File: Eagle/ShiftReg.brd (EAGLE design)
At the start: 100 x 80 mm, 194 parts, among them Q100 310mA/60V/1.6Ω, Q101 310mA/60V/1.6Ω, Q102 310mA/60V/1.6Ω, Q103 310mA/60V/1.6Ω, Q104 310mA/60V/1.6Ω, Q105 310mA/60V/1.6Ω, Q106 310mA/60V/1.6Ω, Q107 310mA/60V/1.6Ω, Q108 310mA/60V/1.6Ω, Q109 310mA/60V/1.6Ω, Q110 310mA/60V/1.6Ω, Q111 310mA/60V/1.6Ω, Q112 310mA/60V/1.6Ω, Q113 310mA/60V/1.6Ω, Q114 310mA/60V/1.6Ω, Q115 310mA/60V/1.6Ω, Q116 310mA/60V/1.6Ω, Q117 310mA/60V/1.6Ω, Q118 310mA/60V/1.6Ω, Q119 310mA/60V/1.6Ω, Q120 310mA/60V/1.6Ω, Q121 310mA/60V/1.6Ω, Q122 310mA/60V/1.6Ω, Q123 310mA/60V/1.6Ω, Q124 310mA/60V/1.6Ω, Q125 310mA/60V/1.6Ω, Q126 310mA/60V/1.6Ω, Q127 310mA/60V/1.6Ω, Q128 310mA/60V/1.6Ω, Q129 310mA/60V/1.6Ω, Q130 310mA/60V/1.6Ω, Q131 310mA/60V/1.6Ω, Q132 310mA/60V/1.6Ω, Q166 310mA/60V/1.6Ω, Q167 310mA/60V/1.6Ω, Q168 310mA/60V/1.6Ω, Q169 310mA/60V/1.6Ω, Q170 310mA/60V/1.6Ω, Q171 310mA/60V/1.6Ω, Q172 310mA/60V/1.6Ω, Q173 310mA/60V/1.6Ω, Q174 310mA/60V/1.6Ω, Q175 310mA/60V/1.6Ω, Q176 310mA/60V/1.6Ω, Q177 310mA/60V/1.6Ω, Q178 310mA/60V/1.6Ω, Q179 310mA/60V/1.6Ω, Q180 310mA/60V/1.6Ω, Q181 310mA/60V/1.6Ω, Q182 310mA/60V/1.6Ω, Q183 310mA/60V/1.6Ω, Q184 310mA/60V/1.6Ω, Q185 310mA/60V/1.6Ω, Q186 310mA/60V/1.6Ω, Q187 310mA/60V/1.6Ω, Q188 310mA/60V/1.6Ω, Q189 310mA/60V/1.6Ω, Q190 310mA/60V/1.6Ω, Q191 310mA/60V/1.6Ω, Q192 310mA/60V/1.6Ω, Q193 310mA/60V/1.6Ω, Q194 310mA/60V/1.6Ω, Q195 310mA/60V/1.6Ω, Q196 310mA/60V/1.6Ω, Q197 310mA/60V/1.6Ω, Q198 310mA/60V/1.6Ω, Q232 310mA/60V/1.6Ω, Q233 310mA/60V/1.6Ω, Q234 310mA/60V/1.6Ω, Q235 310mA/60V/1.6Ω, Q236 310mA/60V/1.6Ω, Q237 310mA/60V/1.6Ω, Q238 310mA/60V/1.6Ω, Q239 310mA/60V/1.6Ω, Q240 310mA/60V/1.6Ω, Q241 310mA/60V/1.6Ω, Q242 310mA/60V/1.6Ω, Q243 310mA/60V/1.6Ω, Q244 310mA/60V/1.6Ω, Q245 310mA/60V/1.6Ω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

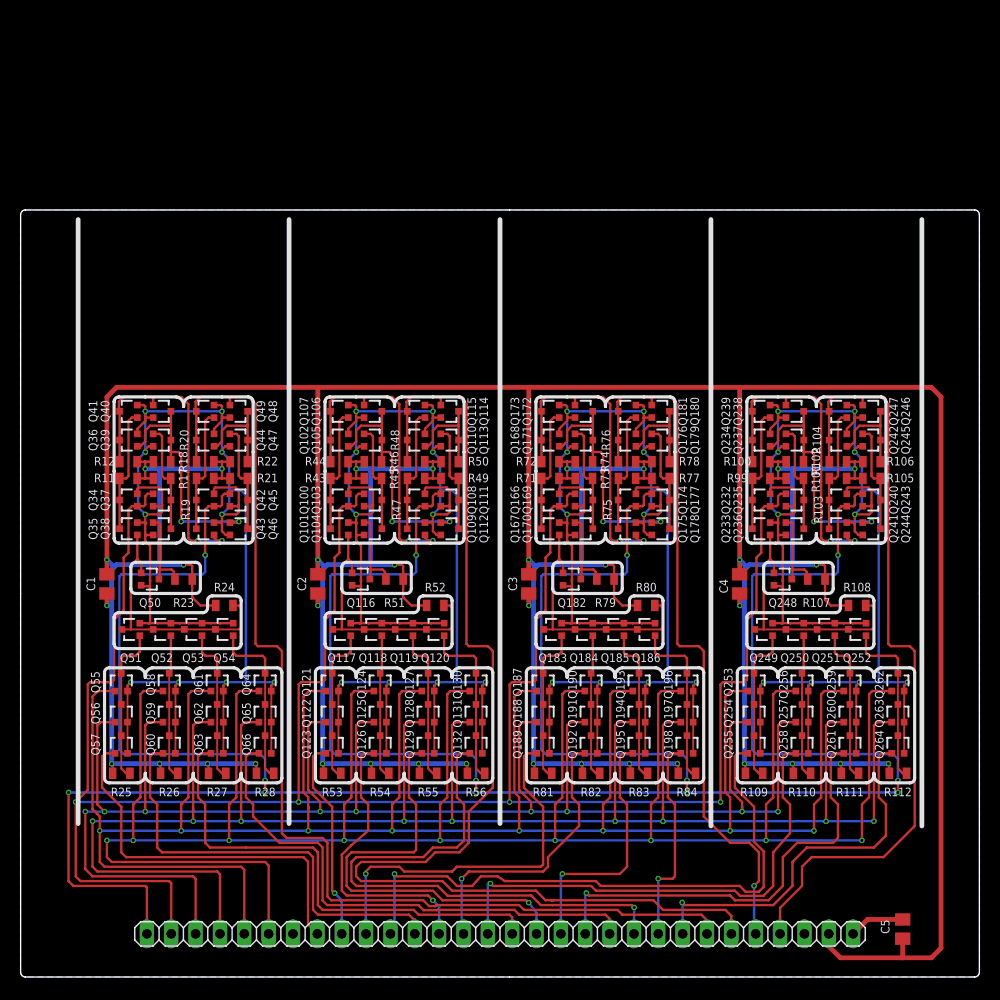
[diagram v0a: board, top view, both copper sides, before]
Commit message: Rerouted for SOT23
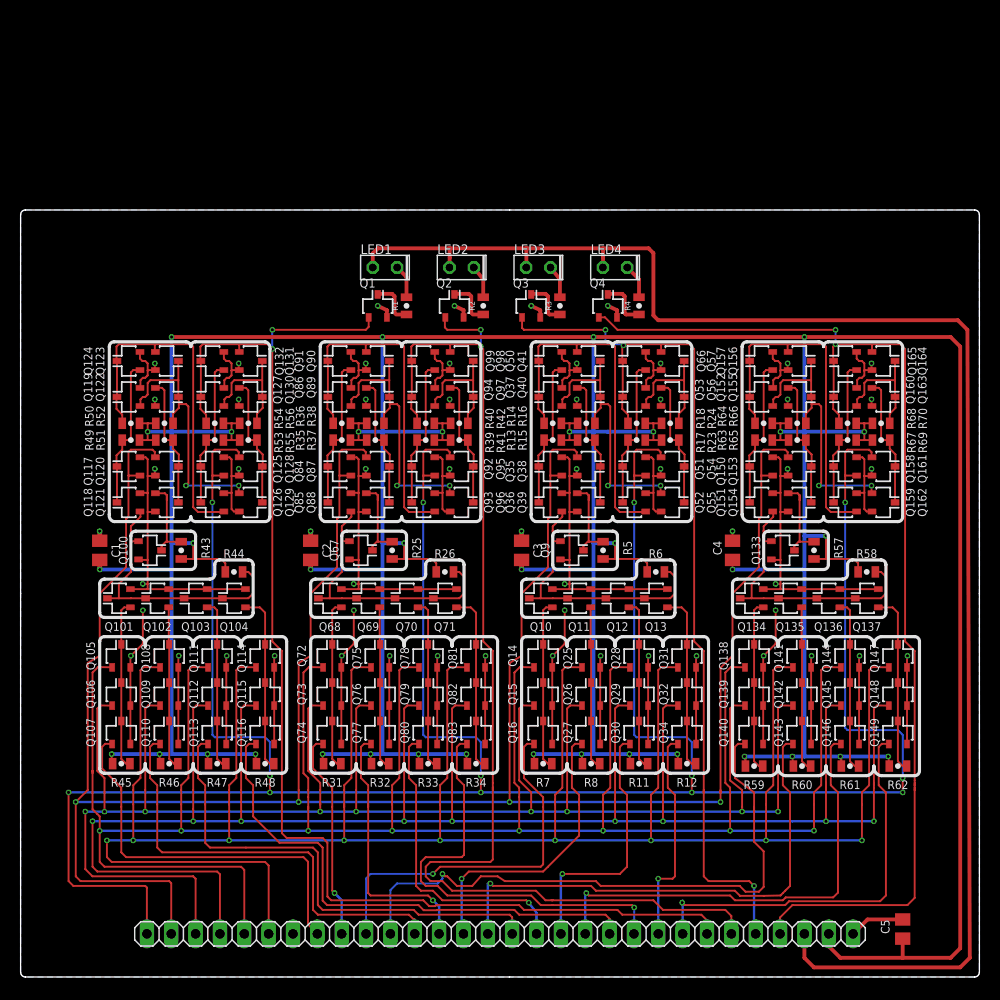
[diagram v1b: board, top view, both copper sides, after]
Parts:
- removed Q166, Q167, Q168, Q169, Q170, Q171, Q172, Q173, Q174, Q175, Q176, Q177, Q178, Q179, Q180, Q181, Q182, Q183, Q184, Q185, Q186, Q187, Q188, Q189, Q190, Q191, Q192, Q193, Q194, Q195, Q196, Q197, Q198, Q232, Q233, Q234, Q235, Q236, Q237, Q238, Q239, Q240, Q241, Q242, Q243, Q244, Q245, Q246, Q247, Q248, Q249, Q250, Q251, Q252, Q253, Q254, Q255, Q256, Q257, Q258, Q259, Q260, Q261, Q262, Q263, Q264, Q42, Q43, Q44, Q45, Q46, Q47, Q48, Q49, Q58, Q59, Q60, Q61, Q62, Q63, Q64, Q65: 310mA/60V/1.6Ω, SparkFun-DiscreteSemi:SOT323
- removed R100, R101, R102, R103, R104, R105, R106, R107, R108, R109, R110, R111, R112, R19, R20, R21, R22, R27, R28, R71, R72, R73, R74, R75, R76, R77, R78, R79, R80, R81, R82, R83, R84, R99: (no value), SparkFun-Resistors:0805
- added LED1, LED2, LED3, LED4: (no value), led:LED2X5
- added Q1, Q2, Q3, Q4: (no value), XSNOR:SOT23
- added Q10, Q11, Q12, Q13, Q133, Q134, Q135, Q136, Q137, Q138, Q139, Q14, Q140, Q141, Q142, Q143, Q144, Q145, Q146, Q147, Q148, Q149, Q15, Q150, Q151, Q152, Q153, Q154, Q155, Q156, Q157, Q158, Q159, Q16, Q160, Q161, Q162, Q163, Q164, Q165, Q25, Q26, Q27, Q28, Q29, Q30, Q31, Q32, Q67, Q68, Q69, Q70, Q71, Q72, Q73, Q74, Q75, Q76, Q77, Q78, Q79, Q80, Q81, Q82, Q83, Q84, Q85, Q86, Q87, Q88, Q89, Q9, Q90, Q91, Q92, Q93, Q94, Q95, Q96, Q97, Q98, Q99: 310mA/60V/1.6Ω, XSNOR:SOT23
- added R1, R13, R14, R15, R16, R2, R3, R31, R32, R33, R34, R35, R36, R37, R38, R39, R4, R40, R41, R42, R5, R57, R58, R59, R6, R60, R61, R62, R63, R64, R65, R66, R67, R68, R69, R7, R70, R8: (no value), XSNOR:0805
- Q100, Q101, Q102, Q103, Q104, Q105, Q106, Q107, Q108, Q109, Q110, Q111, Q112, Q113, Q114, Q115, Q116, Q117, Q118, Q119, Q120, Q121, Q122, Q123, Q124, Q125, Q126, Q127, Q128, Q129, Q130, Q131, Q132, Q34, Q35, Q36, Q37, Q38, Q39, Q40, Q41, Q50, Q51, Q52, Q53, Q54, Q55, Q56, Q57, Q66: device SparkFun-DiscreteSemi:SOT323 -> XSNOR:SOT23
- R11, R12, R17, R18, R23, R24, R25, R26, R43, R44, R45, R46, R47, R48, R49, R50, R51, R52, R53, R54, R55, R56: device SparkFun-Resistors:0805 -> XSNOR:0805
- moved Q57 70.0 mm to (68.0, 64.2), turned to 270 degrees
- moved Q56 66.3 mm to (68.0, 60.5), turned to 270 degrees
- moved R12 66.2 mm to (69.5, 22.2)
- moved Q34 63.1 mm to (69.5, 25.5), turned to 0 degrees
- moved R11 61.0 mm to (64.5, 22.2)
- moved Q55 60.5 mm to (68.0, 49.5), turned to 270 degrees
- moved Q66 55.5 mm to (64.0, 64.2), turned to 90 degrees
- moved Q51 55.2 mm to (64.0, 53.2)
- moved R23 52.8 mm to (67.8, 56.0)
- moved Q53 52.0 mm to (64.0, 60.5)
- moved Q52 51.0 mm to (64.0, 49.5)
- moved R24 50.2 mm to (67.8, 57.8), turned to 180 degrees
- moved Q54 49.7 mm to (68.0, 53.2), turned to 270 degrees
- moved R17 49.7 mm to (64.2, 56.0), turned to 0 degrees
- moved R18 49.7 mm to (64.2, 57.8), turned to 0 degrees
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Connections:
- removed net /Q0A1: Q36.1, Q39.3, Q40.3, Q46.1, R18.1
- removed net /Q0B: Q44.1, Q47.3, Q48.3, R22.1
- removed net /Q1A3: Q102.1, Q105.3, Q106.3, Q112.1, R46.1
- removed net /Q1B: Q110.1, Q113.3, Q114.3, R50.1
- removed net /Q2A5: Q168.1, Q171.3, Q172.3, Q178.1, R74.1
- removed net /Q2B: Q176.1, Q179.3, Q180.3, R78.1
- removed net /Q3A7: Q234.1, Q237.3, Q238.3, Q244.1, R102.1
- removed net /Q3B: Q242.1, Q245.3, Q246.3, R106.1
- removed net AUX1A': Q120.1, Q130.3, Q131.3, Q132.3, R56.2
- removed net LOAD1A': Q119.1, Q127.3, Q128.3, Q129.3, R55.2
- removed net N$116: Q243.3, Q244.3, Q245.1, R105.1
- removed net N$3: JP2.28
- removed net N$49: Q100.3, Q101.3, Q107.1, R43.1
- removed net N$50: Q103.3, Q104.3, Q105.1, R45.1
- removed net N$51: Q108.3, Q109.3, Q115.1, R47.1
- removed net N$52: Q111.3, Q112.3, Q113.1, R49.1
- removed net N$81: Q166.3, Q167.3, Q173.1, R71.1
- removed net N$82: Q169.3, Q170.3, Q171.1, R73.1
- removed net N$83: Q174.3, Q175.3, Q181.1, R75.1
- removed net N$84: Q177.3, Q178.3, Q179.1, R77.1
- removed net Q0A1: Q36.3, Q40.1, Q41.3, Q43.1, R12.1
- removed net Q1A3: Q102.3, Q106.1, Q107.3, Q109.1, R44.1
- removed net Q2A5: Q168.3, Q172.1, Q173.3, Q175.1, R72.1
- removed net Q3A7: Q234.3, Q238.1, Q239.3, Q241.1, R100.1
- removed net R0A: Q38.1, Q50.3, R23.2
- removed net S0A: Q35.1, Q50.1, Q51.3, Q52.3, Q53.3, Q54.3, R24.2
- new net AUX1A'-: Q71.1, Q81.3, Q82.3, Q83.3, R34.2
- new net LED+: JP2.28, LED1.A, LED2.A, LED3.A, LED4.A
- new net LOAD1A'-: Q70.1, Q78.3, Q79.3, Q80.3, R33.2
- new net N$10: Q92.3, Q93.3, Q99.1, R39.1
- new net N$100: Q119.3, Q123.1, Q124.3, Q126.1, R50.1
- new net N$101: Q119.1, Q122.3, Q123.3, Q129.1, R52.1
- new net N$102: Q127.1, Q130.3, Q131.3, R56.1
- new net N$103: Q86.1, Q89.3, Q90.3, Q96.1, R38.1
- new net N$104: Q86.3, Q90.1, Q91.3, Q93.1, R36.1
- new net N$105: Q94.1, Q97.3, Q98.3, R42.1
- new net N$11: Q95.3, Q96.3, Q97.1, R41.1
- new net N$110: Q53.1, Q56.3, Q57.3, R24.1
- new net N$111: Q37.1, Q40.3, Q41.3, Q55.1, R16.1
- new net N$112: Q37.3, Q41.1, Q50.3, Q52.1, R14.1
- new net N$12: Q150.3, Q151.3, Q157.1, R63.1
- new net N$13: Q153.3, Q154.3, Q155.1, R65.1
- new net N$14: Q158.3, Q159.3, Q165.1, R67.1
- new net N$15: Q161.3, Q162.3, Q163.1, R69.1
- new net N$16: Q117.3, Q118.3, Q124.1, R49.1
- new net N$17: Q120.3, Q121.3, Q122.1, R51.1
- new net N$18: Q125.3, Q126.3, Q132.1, R53.1
- new net N$19: Q128.3, Q129.3, Q130.1, R55.1
- new net N$2: Q38.3, Q39.3, Q40.1, R15.1
- new net N$20: Q3.3, R3.1
- new net N$21: Q4.3, R4.1
- new net N$22: LED4.K, R4.2
- new net N$23: LED3.K, R3.2
- new net N$24: LED2.K, R2.2
- new net N$25: LED1.K, R1.2
- new net N$7: Q54.3, Q55.3, Q56.1, R23.1
- new net N$8: Q84.3, Q85.3, Q91.1, R35.1
- new net N$9: Q87.3, Q88.3, Q89.1, R37.1
- new net R0A-: Q100.3, Q121.1, R43.2
- new net S0A-: Q100.1, Q101.3, Q102.3, Q103.3, Q104.3, Q118.1, R44.2
- net /CLK: now also Q117.1, Q120.1, Q150.1, Q153.1, Q35.1, Q38.1, Q84.1, Q87.1; no longer Q100.1, Q103.1, Q166.1, Q169.1, Q232.1, Q235.1, Q34.1, Q37.1
- net /OP1: now also Q112.1, Q115.1, Q145.1, Q148.1, Q29.1, Q32.1, Q79.1, Q82.1; no longer Q128.1, Q131.1, Q194.1, Q197.1, Q260.1, Q263.1, Q62.1, Q65.1
- net /OP2: now also Q108.1, Q114.1, Q141.1, Q147.1, Q25.1, Q31.1, Q75.1, Q81.1; no longer Q124.1, Q130.1, Q190.1, Q196.1, Q256.1, Q262.1, Q58.1, Q64.1
- net AUX0: now also Q116.1; no longer Q66.1
- net AUX0A': now also Q104.1, Q114.3, Q115.3, Q116.3, R48.2; no longer Q54.1, Q64.3, Q65.3, Q66.3, R28.2
- net AUX1: now also Q83.1; no longer Q132.1
- net AUX2: now also Q34.1; no longer Q198.1
- net AUX2A': now also Q13.1, Q31.3, Q32.3, Q34.3, R12.2; no longer Q186.1, Q196.3, Q197.3, Q198.3, R84.2
- net AUX3: now also Q149.1; no longer Q264.1
- net AUX3A': now also Q137.1, Q147.3, Q148.3, Q149.3, R62.2; no longer Q252.1, Q262.3, Q263.3, Q264.3, R112.2
- net CLK: now also Q125.1, Q128.1, Q158.1, Q161.1, Q51.1, Q54.1, Q92.1, Q95.1; no longer Q108.1, Q111.1, Q174.1, Q177.1, Q240.1, Q243.1, Q42.1, Q45.1
- net GND: now also Q1.2, Q10.2, Q11.2, Q12.2, Q13.2, Q133.2, Q134.2, Q135.2, Q136.2, Q137.2, Q138.2, Q139.2, Q14.2, Q140.2, Q141.2, Q142.2, Q143.2, Q144.2, Q145.2, Q146.2, Q147.2, Q148.2, Q149.2, Q15.2, Q150.2, Q151.2, Q152.2, Q153.2, Q154.2, Q155.2, Q156.2, Q157.2, Q158.2, Q159.2, Q16.2, Q160.2, Q161.2, Q162.2, Q163.2, Q164.2, Q165.2, Q2.2, Q25.2, Q26.2, Q27.2, Q28.2, Q29.2, Q3.2, Q30.2, Q31.2, Q32.2, Q4.2, Q67.2, Q68.2, Q69.2, Q70.2, Q71.2, Q72.2, Q73.2, Q74.2, Q75.2, Q76.2, Q77.2, Q78.2, Q79.2, Q80.2, Q81.2, Q82.2, Q83.2, Q84.2, Q85.2, Q86.2, Q87.2, Q88.2, Q89.2, Q9.2, Q90.2, Q91.2, Q92.2, Q93.2, Q94.2, Q95.2, Q96.2, Q97.2, Q98.2, Q99.2; no longer Q166.2, Q167.2, Q168.2, Q169.2, Q170.2, Q171.2, Q172.2, Q173.2, Q174.2, Q175.2, Q176.2, Q177.2, Q178.2, Q179.2, Q180.2, Q181.2, Q182.2, Q183.2, Q184.2, Q185.2, Q186.2, Q187.2, Q188.2, Q189.2, Q190.2, Q191.2, Q192.2, Q193.2, Q194.2, Q195.2, Q196.2, Q197.2, Q198.2, Q232.2, Q233.2, Q234.2, Q235.2, Q236.2, Q237.2, Q238.2, Q239.2, Q240.2, Q241.2, Q242.2, Q243.2, Q244.2, Q245.2, Q246.2, Q247.2, Q248.2, Q249.2, Q250.2, Q251.2, Q252.2, Q253.2, Q254.2, Q255.2, Q256.2, Q257.2, Q258.2, Q259.2, Q260.2, Q261.2, Q262.2, Q263.2, Q264.2, Q42.2, Q43.2, Q44.2, Q45.2, Q46.2, Q47.2, Q48.2, Q49.2, Q58.2, Q59.2, Q60.2, Q61.2, Q62.2, Q63.2, Q64.2, Q65.2
- net LOAD0: now also Q113.1; no longer Q63.1
- net LOAD0A': now also Q103.1, Q111.3, Q112.3, Q113.3, R47.2; no longer Q53.1, Q61.3, Q62.3, Q63.3, R27.2
- net LOAD1: now also Q80.1; no longer Q129.1
- net LOAD2: now also Q30.1; no longer Q195.1
- net LOAD2A': now also Q12.1, Q28.3, Q29.3, Q30.3, R11.2; no longer Q185.1, Q193.3, Q194.3, Q195.3, R83.2
- net LOAD3: now also Q146.1; no longer Q261.1
- net LOAD3A': now also Q136.1, Q144.3, Q145.3, Q146.3, R61.2; no longer Q251.1, Q259.3, Q260.3, Q261.3, R111.2
- net N$1: now also Q36.3, Q50.1, R13.1; no longer Q34.3, Q41.1, R11.1
- net N$113: now also Q160.1, Q163.3, Q164.3, R70.1; no longer Q232.3, Q233.3, Q239.1, R99.1
- net N$114: now also Q152.1, Q155.3, Q156.3, Q162.1, R66.1; no longer Q235.3, Q236.3, Q237.1, R101.1
- net N$115: now also Q152.3, Q156.1, Q157.3, Q159.1, R64.1; no longer Q240.3, Q241.3, Q247.1, R103.1
- net N$4: now also Q51.3, Q52.3, Q66.1; no longer Q37.3, Q38.3, Q39.1
- net N$5: now also Q1.3, R1.1; no longer Q42.3, Q43.3, Q49.1, R19.1
- net N$6: now also Q2.3, R2.1; no longer Q45.3, Q46.3, Q47.1, R21.1
- net NEXT0: now also Q110.1; no longer Q60.1
- net NEXT0A': now also Q102.1, Q108.3, Q109.3, Q110.3, R46.2; no longer Q52.1, Q58.3, Q59.3, Q60.3, R26.2
- net NEXT1: now also Q77.1; no longer Q126.1
- net NEXT1A': now also Q69.1, Q75.3, Q76.3, Q77.3, R32.2; no longer Q118.1, Q124.3, Q125.3, Q126.3, R54.2
- net NEXT2: now also Q27.1; no longer Q192.1
- net NEXT2A': now also Q11.1, Q25.3, Q26.3, Q27.3, R8.2; no longer Q184.1, Q190.3, Q191.3, Q192.3, R82.2
- net NEXT3: now also Q143.1; no longer Q258.1
- net NEXT3A': now also Q135.1, Q141.3, Q142.3, Q143.3, R60.2; no longer Q250.1, Q256.3, Q257.3, Q258.3, R110.2
- net OP1: now also Q106.1, Q109.1, Q139.1, Q142.1, Q15.1, Q26.1, Q73.1, Q76.1; no longer Q122.1, Q125.1, Q188.1, Q191.1, Q254.1, Q257.1, Q56.1, Q59.1
- net OP2: now also Q105.1, Q111.1, Q138.1, Q14.1, Q144.1, Q28.1, Q72.1, Q78.1; no longer Q121.1, Q127.1, Q187.1, Q193.1, Q253.1, Q259.1, Q55.1, Q61.1
- net OUT0: now also Q1.1, Q127.3, Q131.1, Q132.3, R54.1; no longer Q44.3, Q48.1, Q49.3, R20.1
- net OUT1: now also Q2.1, Q94.3, Q98.1, Q99.3, R40.1; no longer Q110.3, Q114.1, Q115.3, R48.1
- net OUT2: now also Q3.1, Q53.3, Q57.1, Q66.3, R18.1; no longer Q176.3, Q180.1, Q181.3, R76.1
- net OUT3: now also Q160.3, Q164.1, Q165.3, Q4.1, R68.1; no longer Q242.3, Q246.1, Q247.3, R104.1
- net PREV0: now also Q107.1; no longer Q57.1
- net PREV0A': now also Q101.1, Q105.3, Q106.3, Q107.3, R45.2; no longer Q51.1, Q55.3, Q56.3, Q57.3, R25.2
- net PREV1: now also Q74.1; no longer Q123.1
- net PREV1A': now also Q68.1, Q72.3, Q73.3, Q74.3, R31.2; no longer Q117.1, Q121.3, Q122.3, Q123.3, R53.2
- net PREV2: now also Q16.1; no longer Q189.1
- net PREV2A': now also Q10.1, Q14.3, Q15.3, Q16.3, R7.2; no longer Q183.1, Q187.3, Q188.3, Q189.3, R81.2
- net PREV3: now also Q140.1; no longer Q255.1
- net PREV3A': now also Q134.1, Q138.3, Q139.3, Q140.3, R59.2; no longer Q249.1, Q253.3, Q254.3, Q255.3, R109.2
- net R1A: now also Q67.3, Q88.1, R25.2; no longer Q104.1, Q116.3, R51.2
- net R2A: now also Q39.1, Q9.3, R5.2; no longer Q170.1, Q182.3, R79.2
- net R3A: now also Q133.3, Q154.1, R57.2; no longer Q236.1, Q248.3, R107.2
- net S1A: now also Q67.1, Q68.3, Q69.3, Q70.3, Q71.3, Q85.1, R26.2; no longer Q101.1, Q116.1, Q117.3, Q118.3, Q119.3, Q120.3, R52.2
- net S2A: now also Q10.3, Q11.3, Q12.3, Q13.3, Q36.1, Q9.1, R6.2; no longer Q167.1, Q182.1, Q183.3, Q184.3, Q185.3, Q186.3, R80.2
- net S3A: now also Q133.1, Q134.3, Q135.3, Q136.3, Q137.3, Q151.1, R58.2; no longer Q233.1, Q248.1, Q249.3, Q250.3, Q251.3, Q252.3, R108.2
- net VCC: now also R11.1, R12.1, R13.2, R14.2, R15.2, R16.2, R23.2, R24.2, R31.1, R32.1, R33.1, R34.1, R35.2, R36.2, R37.2, R38.2, R39.2, R40.2, R41.2, R42.2, R43.1, R44.1, R45.1, R46.1, R47.1, R48.1, R5.1, R51.2, R52.2, R53.2, R54.2, R55.2, R56.2, R57.1, R58.1, R59.1, R6.1, R60.1, R61.1, R62.1, R63.2, R64.2, R65.2, R66.2, R67.2, R68.2, R69.2, R7.1, R70.2, R8.1; no longer R100.2, R101.2, R102.2, R103.2, R104.2, R105.2, R106.2, R107.1, R108.1, R109.1, R11.2, R110.1, R111.1, R112.1, R12.2, R19.2, R20.2, R21.2, R22.2, R23.1, R24.1, R27.1, R28.1, R43.2, R44.2, R45.2, R46.2, R47.2, R48.2, R51.1, R52.1, R53.1, R54.1, R55.1, R56.1, R71.2, R72.2, R73.2, R74.2, R75.2, R76.2, R77.2, R78.2, R79.1, R80.1, R81.1, R82.1, R83.1, R84.1, R99.2
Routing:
- net GND: track 630.5 -> 403.3 mm, vias 44 -> 56
- net LED+: track 0.00 -> 163.1 mm
- net VCC: track 616.4 -> 564.1 mm, vias 32 -> 36
- net CLK: track 335.5 -> 292.7 mm
- net N$112: track 0.00 -> 37.6 mm
- net N$104: track 0.00 -> 37.6 mm
- net N$100: track 0.00 -> 37.6 mm
- net OUT3: track 82.0 -> 118.4 mm, vias 0 -> 2
- net Q2A5: track 34.1 -> 0.00 mm, vias 2 -> 0
- net Q1A3: track 34.1 -> 0.00 mm, vias 2 -> 0
- net Q0A1: track 34.1 -> 0.00 mm, vias 2 -> 0
- net Q3A7: track 34.1 -> 0.00 mm, vias 2 -> 0
- net S0A-: track 0.00 -> 29.4 mm
- net N$101: track 0.00 -> 28.8 mm, vias 0 -> 2
- net N$111: track 0.00 -> 28.8 mm, vias 0 -> 2
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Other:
- board text added: "Universal Shiftregister rev 1"

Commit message: Cleanups of PCBs
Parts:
- JP2: device pinhead:1X30 -> XSNOR:1X30
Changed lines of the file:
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@@
 </autorouter>
 <elements>
-<element name="JP2" library="pinhead" library_urn="urn:adsk.eagle:library:325" package="1X30" package3d_urn="urn:adsk.eagle:package:22460/2" value="" x="50" y="4.5" smashed="yes">
+<element name="JP2" library="XSNOR" library_urn="urn:adsk.eagle:library:1320997" package="1X30" package3d_urn="urn:adsk.eagle:package:1346145/1" value="" x="50" y="4.5" smashed="yes">
 <attribute name="VALUE" x="11.9" y="1.325" size="1.27" layer="27"/>
 </element>

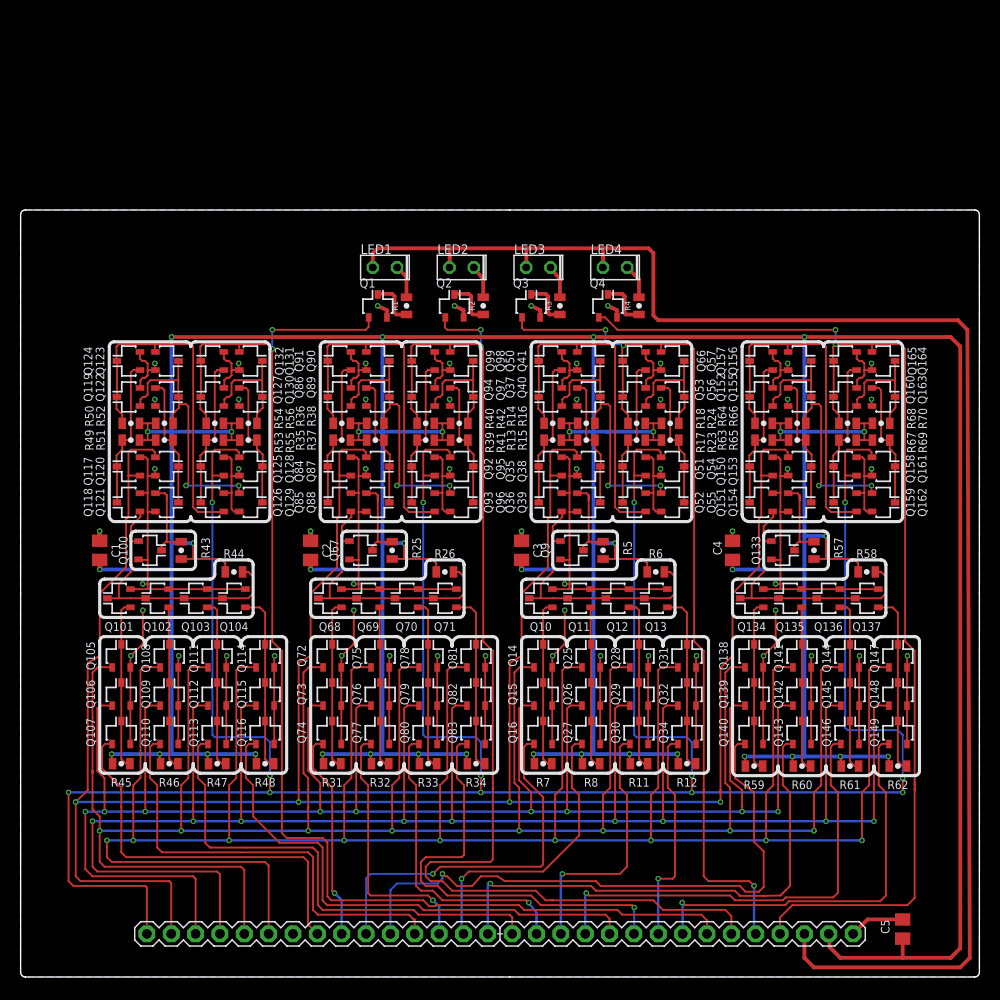
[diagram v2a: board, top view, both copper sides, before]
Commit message: Silk cleanup. Routing of GND instead of floodfill
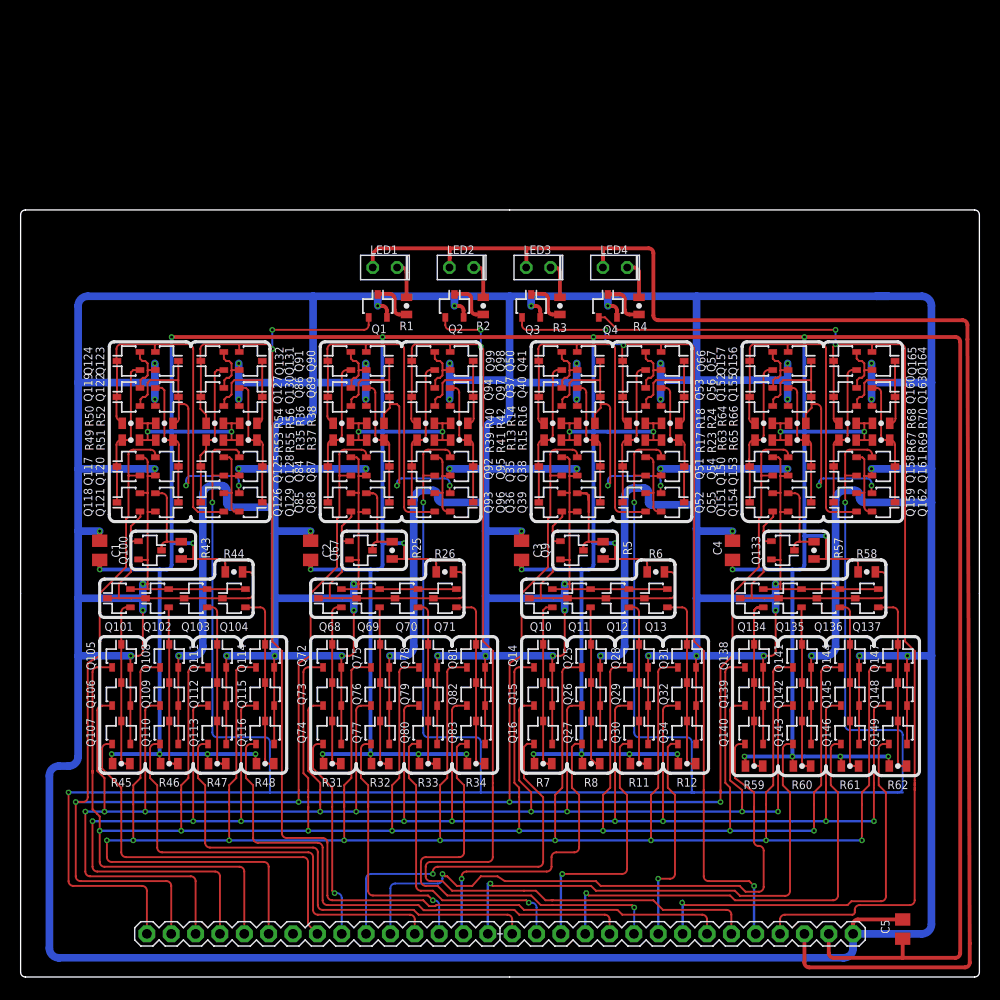
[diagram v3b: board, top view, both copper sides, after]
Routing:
- net GND: track 403.3 -> 1200.5 mm
- net PREV3A': track 17.9 -> 22.6 mm
- net R2A: track 9.32 -> 12.1 mm
- net CLK: track 292.7 -> 295.2 mm, vias 13 -> 5
- net NEXT2: track 30.7 -> 32.2 mm
- net N$101: track 28.8 -> 30.1 mm
- net N$111: track 28.8 -> 30.0 mm
- net /OP1: track 214.5 -> 213.3 mm
- net AUX0: track 55.2 -> 56.3 mm
- net OP1: track 197.8 -> 196.8 mm
- net N$103: track 28.8 -> 29.7 mm
- net LED+: track 163.1 -> 164.0 mm
- net /OP2: track 267.3 -> 266.5 mm
- net /CLK: track 263.8 -> 263.0 mm
- net N$114: track 28.8 -> 29.5 mm
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- removed copper zone on layer 16, net GND
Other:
- board text added: "SmallRoomLabs"

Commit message: Updated boards with pcb template
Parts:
- moved LED1 11.0 mm to (38.0, 85.0)
- moved LED2 11.0 mm to (46.0, 85.0)
- moved LED3 11.0 mm to (54.0, 85.0)
- moved LED4 11.0 mm to (62.0, 85.0)
- moved Q1 11.0 mm to (37.2, 81.0)
- moved Q2 11.0 mm to (45.2, 81.0)
- moved Q3 11.0 mm to (53.2, 81.0)
- moved Q4 11.0 mm to (61.2, 81.0)
- moved R1 11.0 mm to (40.2, 81.0)
- moved R2 11.0 mm to (48.2, 81.0)
- moved R3 11.0 mm to (56.2, 81.0)
- moved R4 11.0 mm to (64.5, 81.0)
- moved Q117 10.2 mm to (9.25, 63.2)
- moved Q118 10.2 mm to (9.25, 59.5)
- moved Q119 10.2 mm to (9.25, 70.5)
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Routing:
- net GND: track 1200.5 -> 1333.8 mm
- net /CLK: track 263.0 -> 308.0 mm
- net CLK: track 295.2 -> 339.8 mm
- net OP2: track 252.9 -> 289.9 mm
- net OP1: track 196.8 -> 233.8 mm
- net /OP2: track 266.5 -> 303.5 mm
- net /OP1: track 213.3 -> 250.3 mm
- net VCC: track 563.9 -> 595.9 mm
- net OUT3: track 118.6 -> 136.0 mm
- net OUT0: track 133.7 -> 147.8 mm
- net OUT2: track 96.5 -> 107.2 mm
- net OUT1: track 121.0 -> 129.7 mm
- net LED+: track 164.0 -> 172.0 mm
- net PREV3A': track 22.6 -> 28.6 mm
- net NEXT0: track 46.6 -> 52.0 mm
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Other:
- board size 100 x 80 mm -> 100 x 100 mm
- board text added: "Universal shiftregister rev1"
- board text removed: "Universal Shiftregister rev 1"
